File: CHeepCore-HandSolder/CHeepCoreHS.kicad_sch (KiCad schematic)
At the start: 8 parts, among them J101 Conn_01x10, J102 Conn_01x10, U101 CH32V003FxPx, Y101 Crystal_GND24

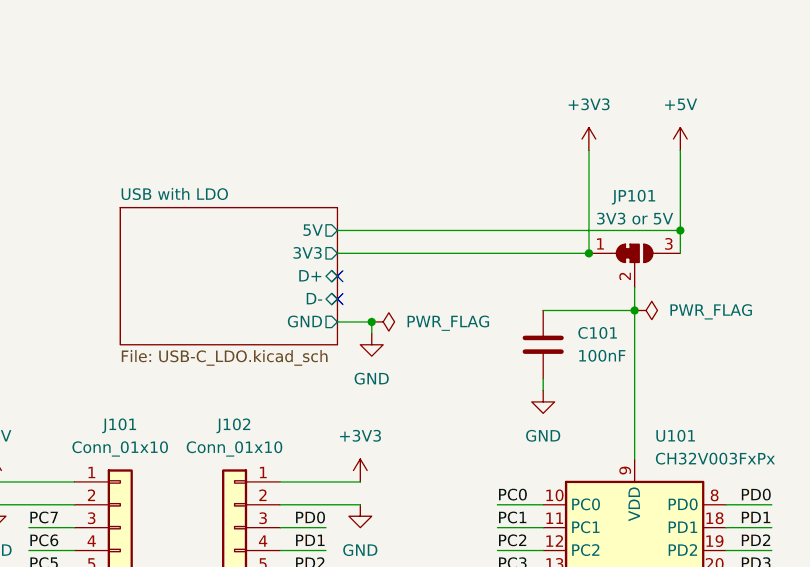
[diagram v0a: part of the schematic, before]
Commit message: Add USB smd pads on the back
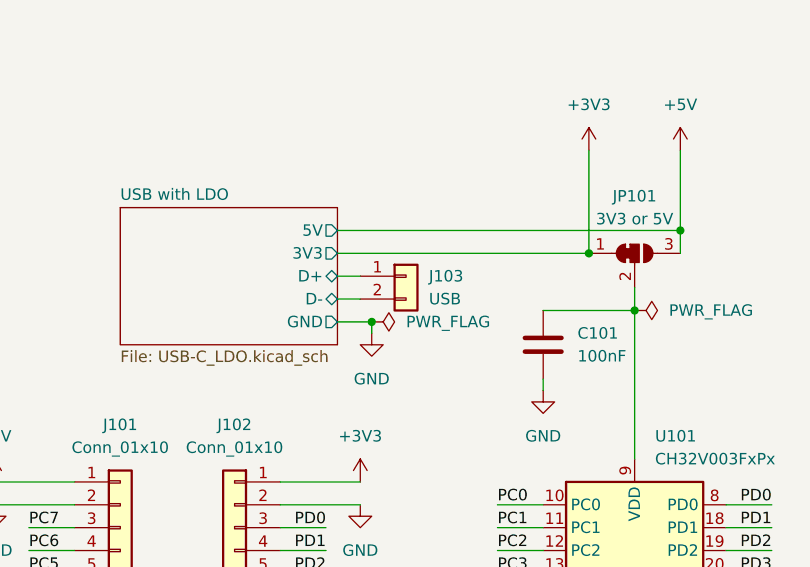
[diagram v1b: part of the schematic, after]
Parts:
- added J103: USB, Connector_PinHeader_1.00mm:PinHeader_2x01_P1.00mm_Vertical_SMD, symbol Connector_Generic:Conn_01x02
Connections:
- net USB with LDO/D+: now also J103.1 (Pin_1)
- net USB with LDO/D-: now also J103.2 (Pin_2)
- no-connect marks 7 -> 5
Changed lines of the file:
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@@
 		(title "CHeepCore")
 		(date "2025-08-06")
-		(rev "0.0.1b")
+		(rev "0.0.1c")
 		(company "VollständigerName")
 		(comment 1 "github.com/VollstaendigerName")
@@
 	)
 	(no_connect
-		(at 90.17 69.85)
-	)
-	(no_connect
 		(at 195.58 140.97)
 	)
@@
 	)
 	(no_connect
-		(at 90.17 67.31)
-	)
-	(no_connect
 		(at 195.58 111.76)
 	)
@@
 	(wire
 		(pts
+			(xy 90.17 67.31) (xy 92.71 67.31)
+		)
+		(stroke
+			(width 0)
+			(type default)
+		)
+	)
+	(wire
+		(pts
 			(xy 156.21 120.65) (xy 147.32 120.65)
 		)
@@
 	(wire
 		(pts
+			(xy 90.17 69.85) (xy 92.71 69.85)
+		)
+		(stroke
+			(width 0)
+			(type default)
+		)
+	)
+	(wire
+		(pts
 			(xy 90.17 62.23) (xy 128.27 62.23)
 		)
@@
 				)
 			)
-			(table_cell ""
+			(table_cell "0.0.1c"
 				(exclude_from_sim no)
 				(at 228.6 20.32 0)
@@
 				)
 			)
-			(table_cell ""
+			(table_cell "Added USB D+ D- to pad"
 				(exclude_from_sim no)
 				(at 243.84 20.32 0)
@@
 					(unit 1)
 				)
+			)
+		)
+	)
+	(symbol
+		(lib_id "Connector_Generic:Conn_01x02")
+		(at 97.79 67.31 0)
+		(unit 1)
+		(exclude_from_sim no)
+		(in_bom yes)
+		(on_board yes)
+		(dnp no)
+		(fields_autoplaced yes)
+		(property "Reference" "J103"
+			(at 100.33 67.3099 0)
+			(effects
+				(font
+					(size 1.27 1.27)
+				)
+				(justify left)
+			)
+		)
+		(property "Value" "USB"
+			(at 100.33 69.8499 0)
+			(effects
+				(font
+					(size 1.27 1.27)
+				)
+				(justify left)
+			)
+		)
+		(property "Footprint" "Connector_PinHeader_1.00mm:PinHeader_2x01_P1.00mm_Vertical_SMD"
+			(at 97.79 67.31 0)
+			(effects
+				(font
+					(size 1.27 1.27)
+				)
+				(hide yes)
+			)
+		)
+		(property "Datasheet" "~"
+			(at 97.79 67.31 0)
+			(effects
+				(font
+					(size 1.27 1.27)
+				)
+				(hide yes)
+			)
+		)
+		(property "Description" "Generic connector, single row, 01x02, script generated (kicad-library-utils/schlib/autogen/connector/)"
+			(at 97.79 67.31 0)
+			(effects
+				(font
+					(size 1.27 1.27)
+				)
+				(hide yes)
+			)
+		)
+		(pin "1"
+		)
+		(pin "2"
+		)
+		(instances
+			(project ""
+				(path "/1a6f5452-e688-4341-937f-30ed63281f98"
+					(reference "J103")
+					(unit 1)
+				)
